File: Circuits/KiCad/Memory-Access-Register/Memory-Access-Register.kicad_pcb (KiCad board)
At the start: 2 copper layers, 38 parts, among them J1 Conn_01x16_Male, J2 Conn_01x16_Male, J3 Conn_01x16_Male, SW1 SW_DPDT_x2, SW10 SW_DPDT_x2, SW11 SW_DPDT_x2, SW12 SW_DPDT_x2, SW13 SW_DPDT_x2, SW14 SW_DPDT_x2, SW15 SW_DPDT_x2, SW16 SW_DPDT_x2, SW17 SW_DPDT_x2, SW2 SW_DPDT_x2, SW3 SW_DPDT_x2, SW4 SW_DPDT_x2, SW5 SW_DPDT_x2, SW6 SW_DPDT_x2, SW7 SW_DPDT_x2, SW8 SW_DPDT_x2, SW9 SW_DPDT_x2, U1 74x08, U10 74x157, U2 74x245, U3 74x245, U4 74x245, U5 74x377, U6 74x377, U7 74x157, U8 74x157, U9 74x157

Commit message: Work in progress on MAR pcb layout
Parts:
- moved J3 163.1 mm to (254.0, 47.6)
- moved J2 151.6 mm to (227.3, -8.89)
- moved RN3 123.5 mm to (111.8, 12.7), turned to 180 degrees
- moved RN4 106.1 mm to (88.3, 12.7), turned to 180 degrees
- moved BAR1 83.8 mm to (91.4, 24.1), turned to 90 degrees
- moved J1 79.2 mm to (31.1, 11.4)
- moved BAR2 53.9 mm to (65.4, 24.1), turned to 90 degrees

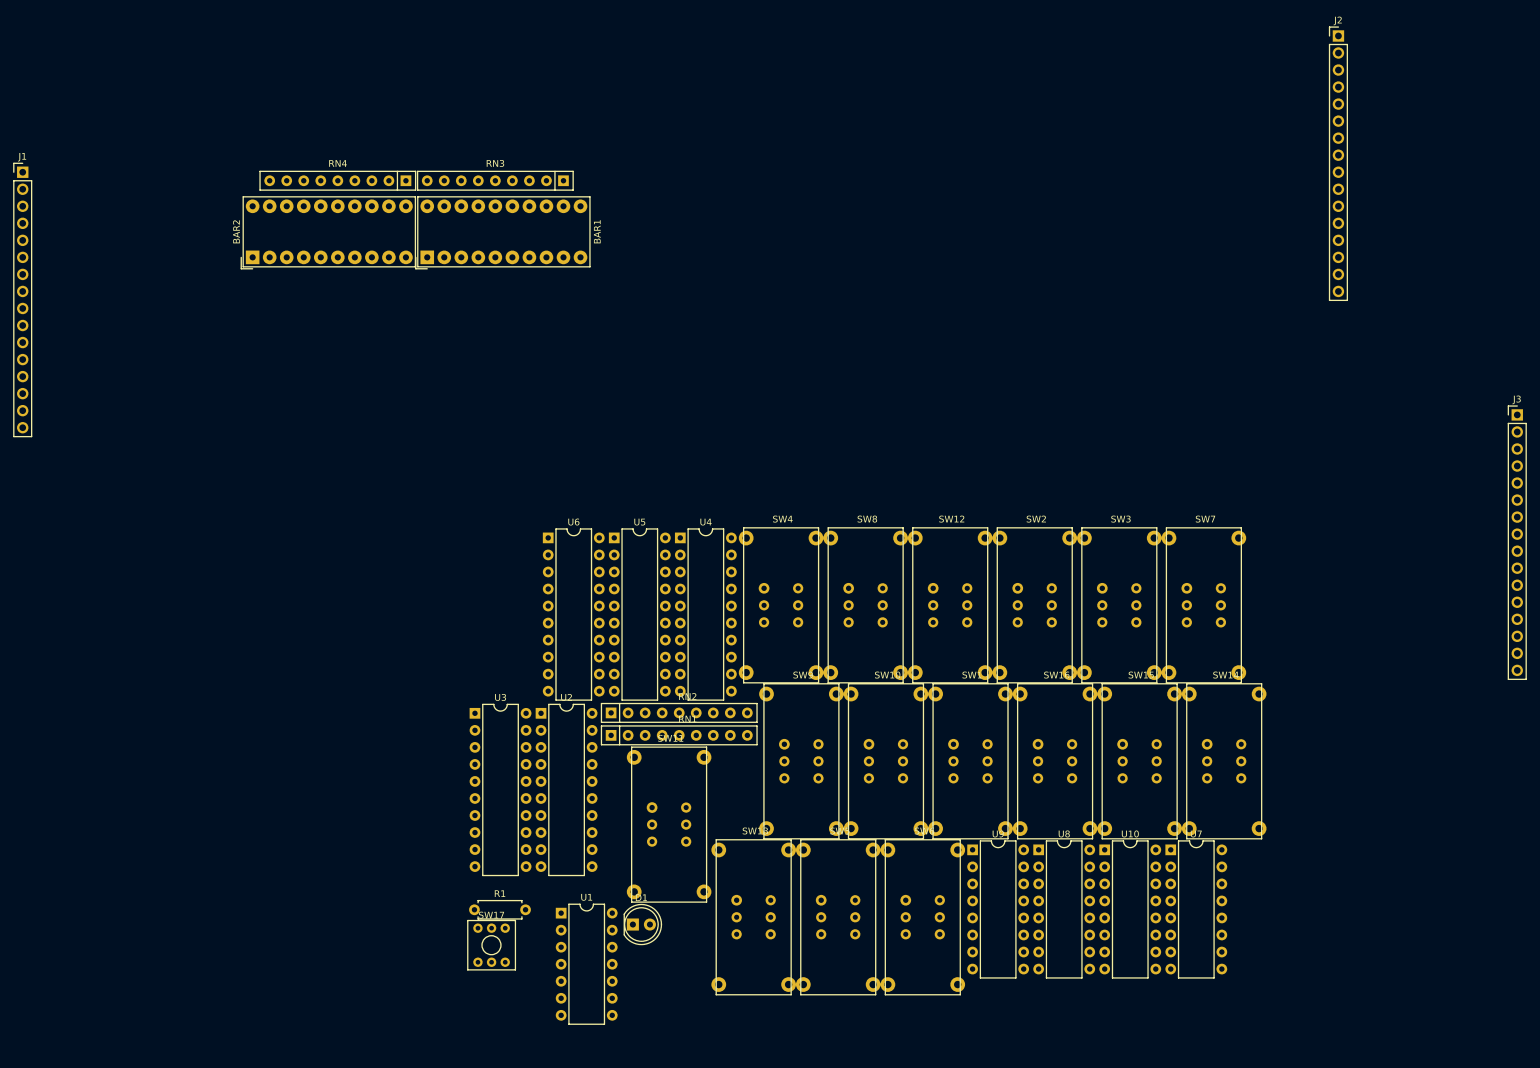
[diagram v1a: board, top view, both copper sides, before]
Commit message: Routed MAR PCB
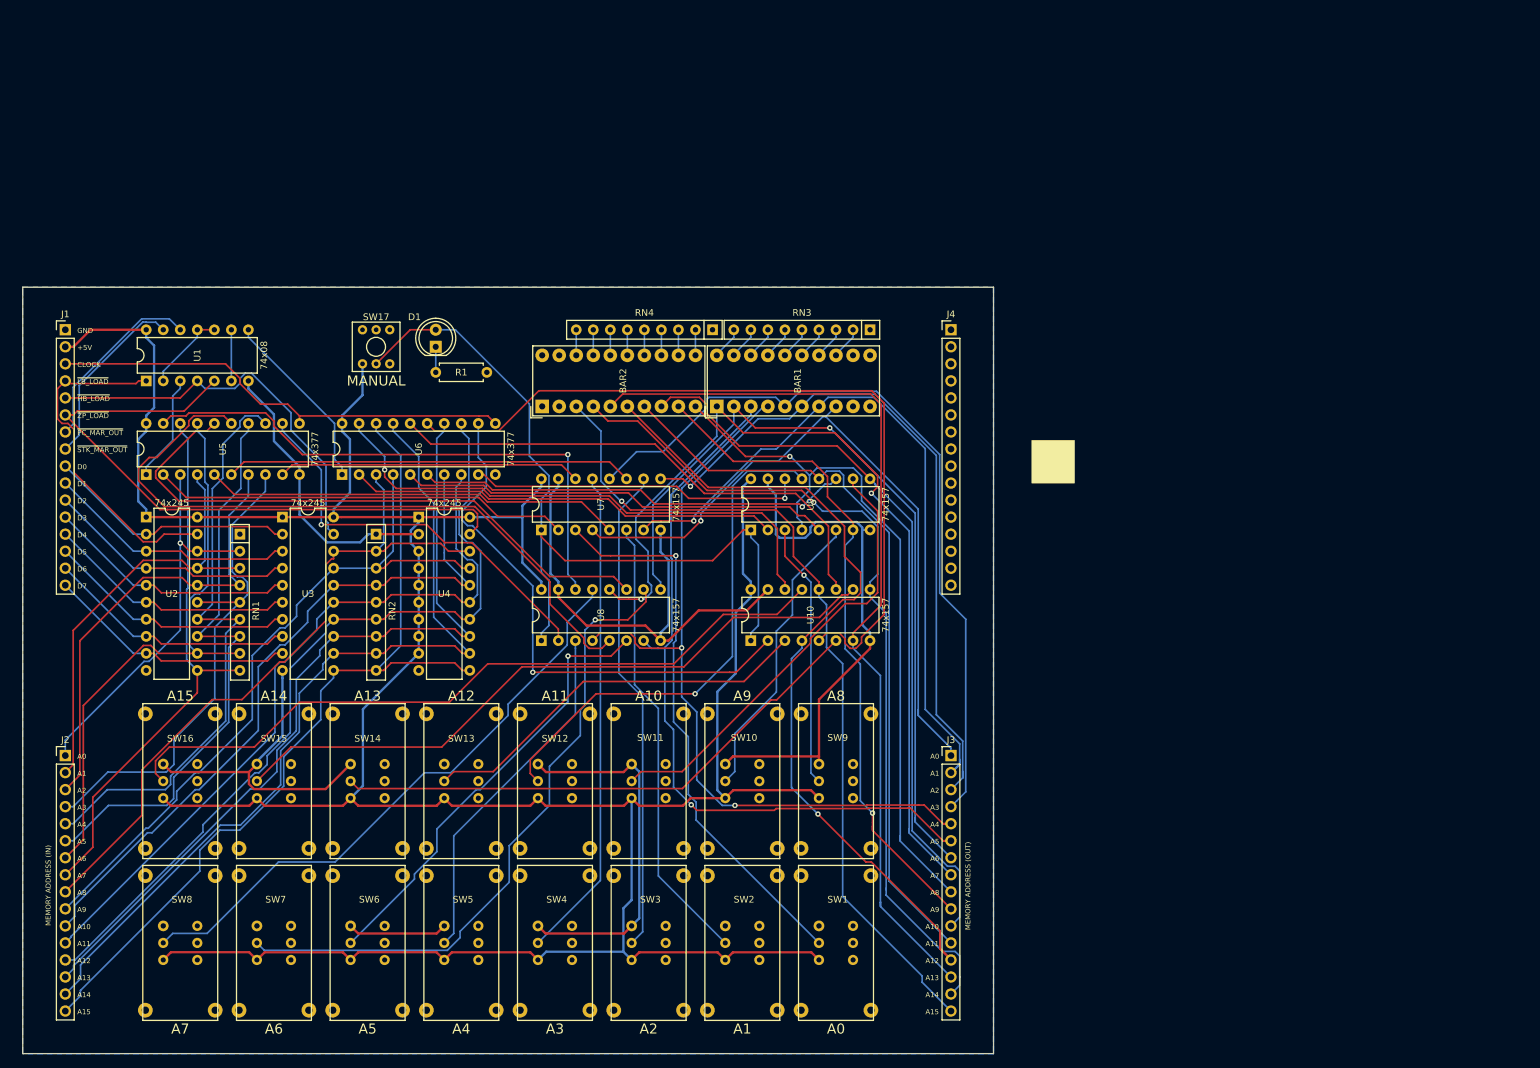
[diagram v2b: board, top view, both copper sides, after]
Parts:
- added J4: Conn_01x16_Male, Connector_PinHeader_2.54mm:PinHeader_1x16_P2.54mm_Vertical, F.Cu at (169.5, 34.9)
- moved J2 218.1 mm to (37.5, 98.4)
- moved SW7 147.5 mm to (68.6, 126.4)
- moved SW16 130.5 mm to (54.6, 102.2)
- moved SW15 129.1 mm to (68.6, 102.2)
- moved SW14 127.8 mm to (82.5, 102.2)
- moved SW8 113.9 mm to (54.6, 126.4)
- moved U7 105.3 mm to (108.5, 64.8), turned to 90 degrees
- moved U1 100.6 mm to (49.5, 42.5), turned to 90 degrees
- moved J3 98.6 mm to (169.5, 98.4)
- moved D1 91.0 mm to (92.7, 37.5), turned to 90 degrees
- moved SW17 90.9 mm to (83.8, 37.5)
- moved SW3 86.4 mm to (124.5, 126.4)
- moved SW6 82.9 mm to (82.5, 126.4)
- moved U8 80.5 mm to (108.5, 81.3), turned to 90 degrees
- moved R1 80.2 mm to (100.3, 41.3), turned to 180 degrees
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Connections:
- U10 pad 10: MANUAL_A15 -> MANUAL_A14
- U10 pad 12: Net-(BAR2-Pad4) -> Net-(BAR2-Pad3)
- U10 pad 13: MANUAL_A14 -> MANUAL_A15
- U10 pad 9: Net-(BAR2-Pad3) -> Net-(BAR2-Pad4)
- U6 pad 16: Net-(U10-Pad14) -> Net-(U10-Pad11)
- U6 pad 19: Net-(U10-Pad11) -> Net-(U10-Pad14)
- U7 pad 10: MANUAL_A3 -> MANUAL_A2
- U7 pad 11: Net-(U5-Pad9) -> Net-(U5-Pad6)
- U7 pad 12: Net-(BAR1-Pad6) -> Net-(BAR1-Pad5)
- U7 pad 13: MANUAL_A2 -> MANUAL_A3
- U7 pad 14: Net-(U5-Pad6) -> Net-(U5-Pad9)
- U7 pad 9: Net-(BAR1-Pad5) -> Net-(BAR1-Pad6)
- U8 pad 10: MANUAL_A7 -> MANUAL_A6
- U8 pad 11: Net-(U5-Pad19) -> Net-(U5-Pad16)
- U8 pad 12: Net-(BAR1-Pad2) -> Net-(BAR1-Pad1)
- U8 pad 13: MANUAL_A6 -> MANUAL_A7
- U8 pad 14: Net-(U5-Pad16) -> Net-(U5-Pad19)
- U8 pad 9: Net-(BAR1-Pad1) -> Net-(BAR1-Pad2)
- U9 pad 10: MANUAL_A11 -> MANUAL_A10
- U9 pad 11: Net-(U6-Pad9) -> Net-(U6-Pad6)
- U9 pad 12: Net-(BAR2-Pad8) -> Net-(BAR2-Pad7)
- U9 pad 13: MANUAL_A10 -> MANUAL_A11
- U9 pad 14: Net-(U6-Pad6) -> Net-(U6-Pad9)
- U9 pad 9: Net-(BAR2-Pad7) -> Net-(BAR2-Pad8)
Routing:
- net +5V: track 0.00 -> 474.2 mm
- net GND: track 0.00 -> 313.7 mm
- net Net-(BAR2-Pad5): track 0.00 -> 135.5 mm
- net Net-(BAR1-Pad1): track 0.00 -> 134.6 mm, vias 0 -> 2
- net Net-(J2-Pad16): track 0.00 -> 130.2 mm
- net Net-(J2-Pad15): track 0.00 -> 129.4 mm
- net Net-(BAR2-Pad4): track 0.00 -> 127.4 mm, vias 0 -> 1
- net Net-(BAR2-Pad3): track 0.00 -> 126.1 mm, vias 0 -> 1
- net Net-(BAR2-Pad6): track 0.00 -> 125.7 mm, vias 0 -> 1
- net Net-(J2-Pad14): track 0.00 -> 123.7 mm
- net Net-(J2-Pad13): track 0.00 -> 122.5 mm
- net MANUAL_INPUT: track 0.00 -> 120.5 mm
- net Net-(BAR1-Pad2): track 0.00 -> 120.5 mm, vias 0 -> 1
- net Net-(BAR1-Pad4): track 0.00 -> 119.3 mm, vias 0 -> 2
- net Net-(U10-Pad5): track 0.00 -> 117.5 mm
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- added copper zone on B.Cu, net GND
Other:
- board outline added: 144.8 x 114.3 mm
- net class Power added: clearance 0.2, trace_width 0.35, via_dia 0.8, via_drill 0.4
- board text added: "+5V"
- board text added: "A0"
- board text added: "A1"
- board text added: "A10"
- board text added: "A11"
- board text added: "A12"
- board text added: "A13"
- board text added: "A14"
- board text added: "A15"
- board text added: "A2"
- board text added: "A3"
- board text added: "A4"
- board text added: "A5"
- board text added: "A6"
- board text added: "A7"
- board text added: "A8"
- board text added: "A9"
- board text added: "CLOCK"
- board text added: "D0"
- board text added: "D1"
- board text added: "D2"
- board text added: "D3"
- board text added: "D4"
- board text added: "D5"
- board text added: "D6"
- board text added: "D7"
- board text added: "GND"
- board text added: "MANUAL"
- board text added: "MEMORY ADDRESS (IN)"
- board text added: "MEMORY ADDRESS (OUT)"
- board text added: "~HB_LOAD"
- board text added: "~LB_LOAD"
- board text added: "~PC_MAR_OUT"
- board text added: "~STK_MAR_OUT"
- board text added: "~ZP_LOAD"

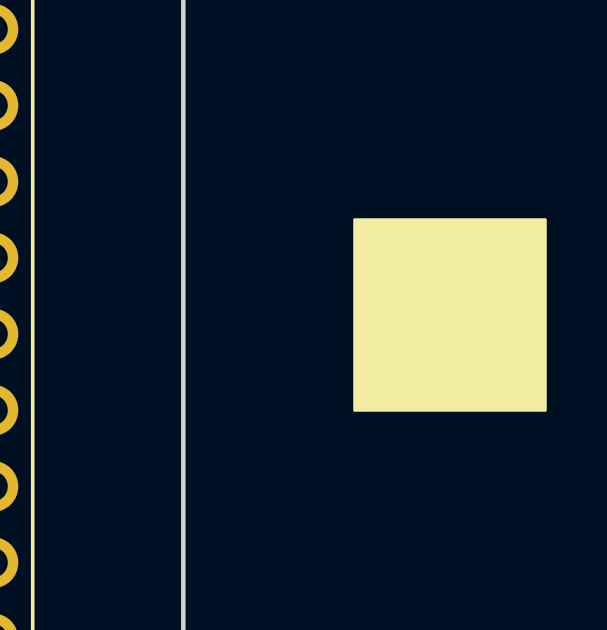
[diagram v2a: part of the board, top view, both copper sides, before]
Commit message: Finished Memory & Memory Access Register PCB
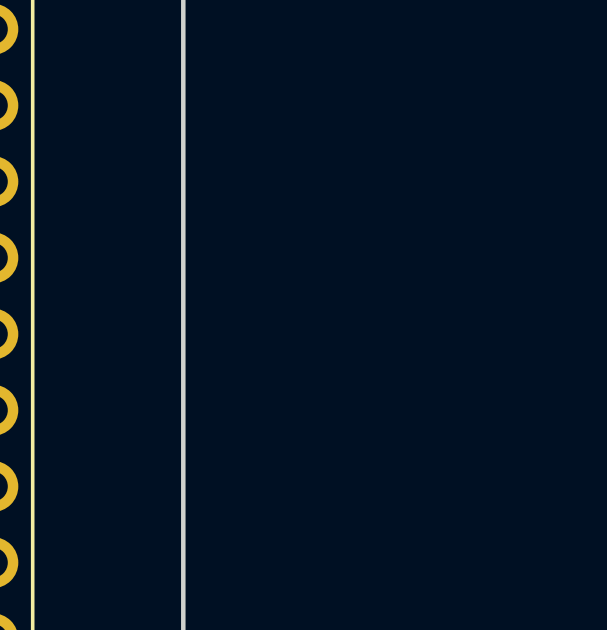
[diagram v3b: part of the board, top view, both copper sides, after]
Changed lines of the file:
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@@
     (pcbplotparams
       (layerselection 0x010fc_ffffffff)
-      (usegerberextensions false)
+      (usegerberextensions true)
       (usegerberattributes false)
       (usegerberadvancedattributes false)
@@
       (outputformat 1)
       (mirror false)
-      (drillshape 1)
+      (drillshape 0)
       (scaleselection 1)
-      (outputdirectory ""))
+      (outputdirectory "gerber/"))
   )
   (net 0 "")
@@
     (effects (font (size 1.5 1.5) (thickness 0.25)))
   )
-  (gr_poly (pts (xy 181.61 57.785) (xy 181.61 51.435) (xy 187.96 51.435) (xy 187.96 57.785)) (layer F.SilkS) (width 0.1))
+  (gr_poly (pts (xy 181.61 57.785) (xy 181.61 51.435) (xy 187.96 51.435) (xy 187.96 57.785)) (layer Margin) (width 0.1))
   (segment (start 66.04 99.695) (end 64.8494 100.8856) (width 0.35) (layer F.Cu) (net 1))
   (segment (start 157.48 64.77) (end 156.3047 64.77) (width 0.35) (layer B.Cu) (net 1))
